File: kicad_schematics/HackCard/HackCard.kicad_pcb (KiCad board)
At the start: 2 copper layers, 43 x 38 mm, 28 parts, among them J10 JST VH B2P, J3 JST VH B4P, J4 Pin Header 2X6, J5 JST VH B4P, J8 JST VH B3P, J9 JST VH B3P, Q1 BC847B, U1 HEF4093B, U2 HEF4093B

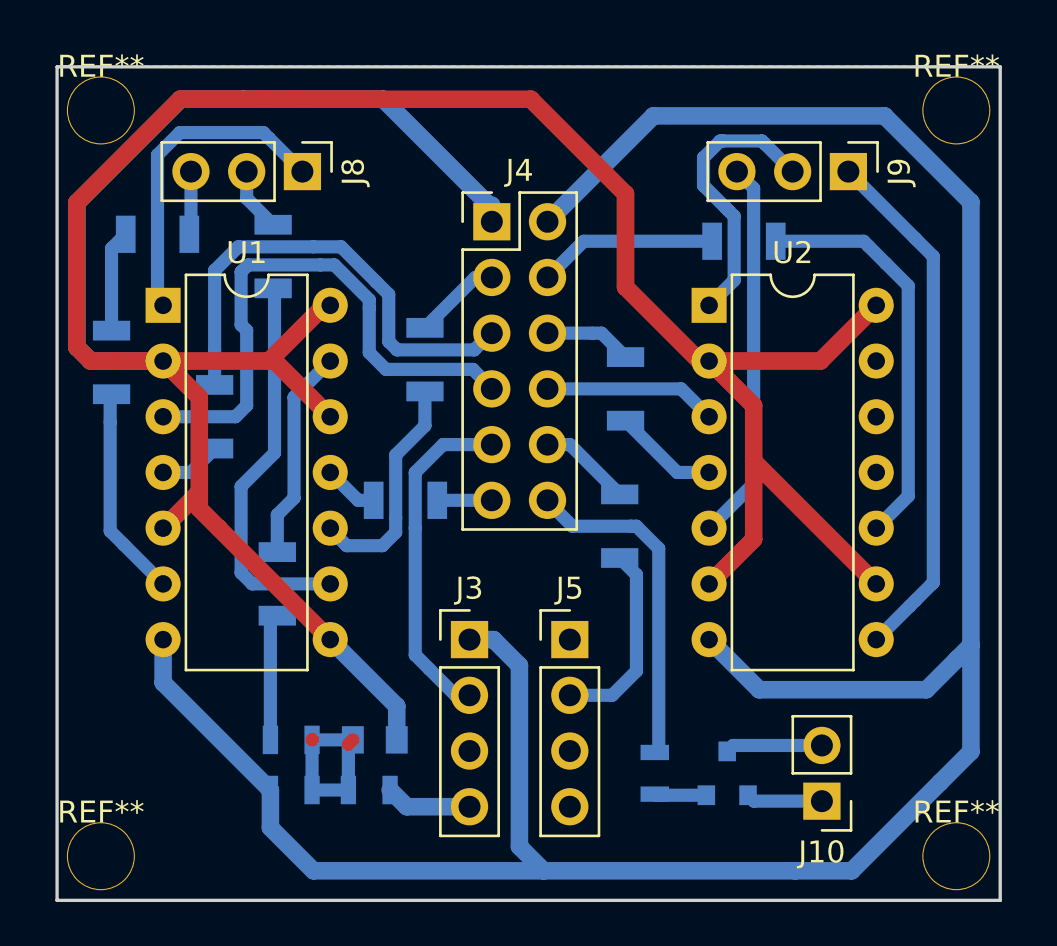
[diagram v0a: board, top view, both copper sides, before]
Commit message: text for I/O
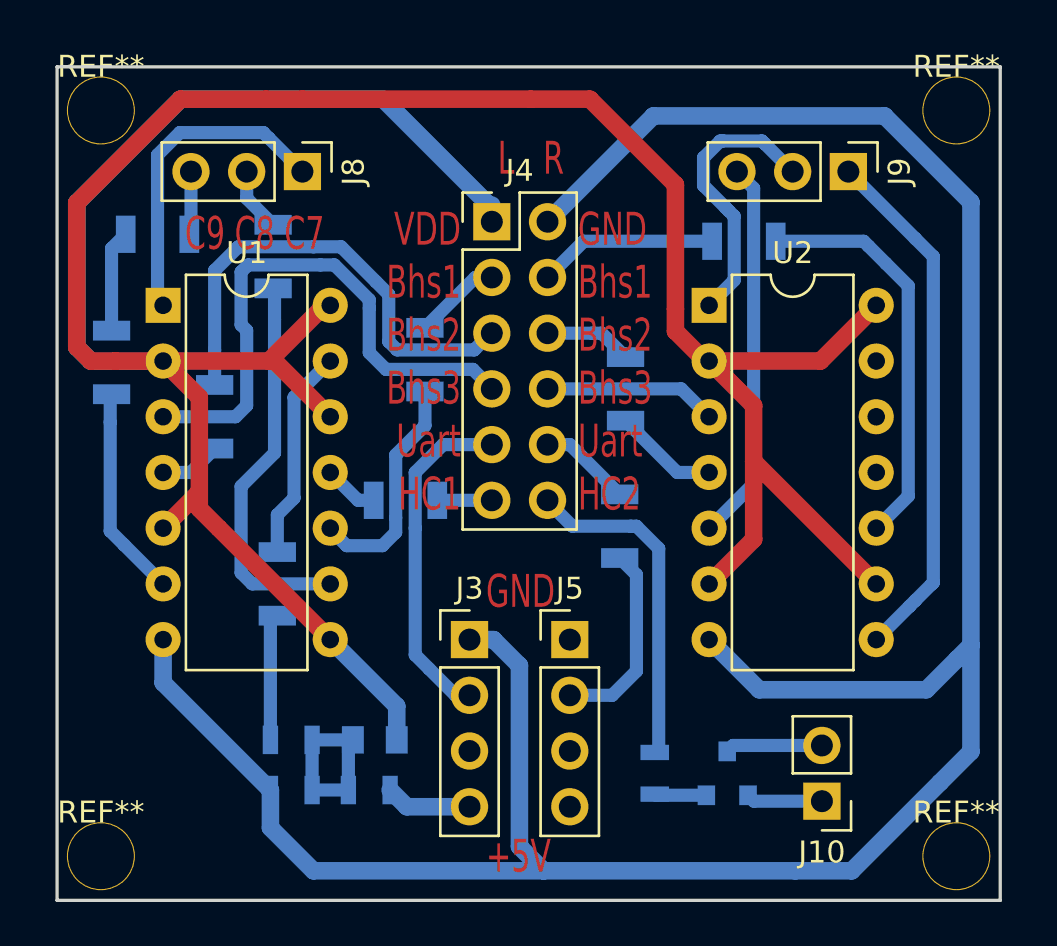
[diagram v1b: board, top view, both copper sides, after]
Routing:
- net VDD: track 149.0 -> 150.9 mm
- removed copper zone on F.Cu, net GND
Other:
- board text added: "C9 C8 C7"
- board text added: "GND +5V"
- board text added: "GND Bhs1 Bhs2 Bhs3 Uart HC2"
- board text added: "L R"
- board text added: "VDD Bhs1 Bhs2 Bhs3 Uart HC1"
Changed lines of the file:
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@@
     (area 96.11657 84.555 168.85943 138.105001)
     (thickness 1.6)
-    (drawings 9)
-    (tracks 213)
+    (drawings 14)
+    (tracks 214)
     (zones 0)
     (modules 28)
@@
     (mod_text_size 1 1)
     (mod_text_width 0.15)
-    (pad_size 3.1 3.1)
-    (pad_drill 3)
+    (pad_size 2 2)
+    (pad_drill 0.8)
     (pad_to_mask_clearance 0.2)
     (aux_axis_origin 0 0)
     (grid_origin 110.988 93.255)
-    (visible_elements FFFEFF7F)
+    (visible_elements FFFCFF7F)
     (pcbplotparams
-      (layerselection 0x00000_80000000)
+      (layerselection 0x00000_00000001)
       (usegerberextensions false)
       (excludeedgelayer false)
@@
       (subtractmaskfromsilk false)
       (outputformat 2)
-      (mirror false)
+      (mirror true)
       (drillshape 2)
       (scaleselection 1)
@@
     (pad 1 thru_hole circle (at 0 0) (size 3.1 3.1) (drill 3) (layers *.Cu *.Mask))
   )
+  (dimension 38 (width 0.3) (layer Eco2.User)
+    (gr_text "38,000 mm" (at 103.638 112.255 90) (layer Eco2.User)
+      (effects (font (size 1.5 1.5) (thickness 0.3)))
+    )
+    (feature1 (pts (xy 110.988 93.255) (xy 102.288 93.255)))
+    (feature2 (pts (xy 110.988 131.255) (xy 102.288 131.255)))
+    (crossbar (pts (xy 104.988 131.255) (xy 104.988 93.255)))
+    (arrow1a (pts (xy 104.988 93.255) (xy 105.574421 94.381504)))
+    (arrow1b (pts (xy 104.988 93.255) (xy 104.401579 94.381504)))
+    (arrow2a (pts (xy 104.988 131.255) (xy 105.574421 130.128496)))
+    (arrow2b (pts (xy 104.988 131.255) (xy 104.401579 130.128496)))
+  )
+  (gr_text "GND\n\n\n\n\n+5V" (at 130.546 123.227) (layer F.Cu)
+    (effects (font (size 1.5 1) (thickness 0.25)) (justify left))
+  )
+  (gr_text "C9 C8 C7" (at 123.18 100.875) (layer F.Cu)
+    (effects (font (size 1.5 1) (thickness 0.25)) (justify right))
+  )
+  (gr_text "L   R" (at 134.102 97.446) (layer F.Cu)
+    (effects (font (size 1.5 1) (thickness 0.25)) (justify right))
+  )
+  (gr_text "GND\nBhs1\nBhs2\nBhs3\nUart\nHC2" (at 134.737 106.717) (layer F.Cu)
+    (effects (font (size 1.5 1) (thickness 0.25)) (justify left))
+  )
+  (gr_text "VDD\nBhs1\nBhs2\nBhs3\nUart\nHC1" (at 129.403 106.717) (layer F.Cu)
+    (effects (font (size 1.5 1) (thickness 0.25)) (justify right))
+  )
   (dimension 3 (width 0.3) (layer Eco2.User)
     (gr_text "3,000 mm" (at 113.488 136.755) (layer Eco2.User)
@@
     (arrow2b (pts (xy 111.488 132.755) (xy 112.614504 132.168579)))
   )
-  (dimension 38 (width 0.3) (layer Eco2.User)
-    (gr_text "38,000 mm" (at 103.638 112.255 270) (layer Eco2.User)
-      (effects (font (size 1.5 1.5) (thickness 0.3)))
-    )
-    (feature1 (pts (xy 110.988 131.255) (xy 102.288 131.255)))
-    (feature2 (pts (xy 110.988 93.255) (xy 102.288 93.255)))
-    (crossbar (pts (xy 104.988 93.255) (xy 104.988 131.255)))
-    (arrow1a (pts (xy 104.988 131.255) (xy 104.401579 130.128496)))
-    (arrow1b (pts (xy 104.988 131.255) (xy 105.574421 130.128496)))
-    (arrow2a (pts (xy 104.988 93.255) (xy 104.401579 94.381504)))
-    (arrow2b (pts (xy 104.988 93.255) (xy 105.574421 94.381504)))
-  )
   (dimension 34 (width 0.3) (layer Eco2.User)
     (gr_text "34,000 mm" (at 106.638 112.255 90) (layer Eco2.User)
@@
   (gr_line (start 153.99 131.268) (end 110.99 131.268) (angle 90) (layer Edge.Cuts) (width 0.15))
   (gr_line (start 153.99 93.268) (end 153.99 131.268) (angle 90) (layer Edge.Cuts) (width 0.15))
-  (segment (start 122.632 123.936) (end 122.616 123.952) (width 0.6) (layer F.Cu) (net 0))
-  (segment (start 124.272 124.156) (end 124.476 123.952) (width 0.6) (layer F.Cu) (net 0))
+  (segment (start 139.182 104.304) (end 139.182 105.32) (width 0.8) (layer F.Cu) (net 1))
+  (segment (start 139.182 105.32) (end 140.542 106.68) (width 0.8) (layer F.Cu) (net 1))
+  (segment (start 140.542 106.68) (end 140.716 106.68) (width 0.8) (layer F.Cu) (net 1))
+  (segment (start 132.578 94.742) (end 135.282 94.742) (width 0.8) (layer F.Cu) (net 1))
+  (segment (start 139.182 98.642) (end 139.182 104.304) (width 0.8) (layer F.Cu) (net 1))
+  (segment (start 135.282 94.742) (end 139.182 98.642) (width 0.8) (layer F.Cu) (net 1))
   (segment (start 120.513 94.742) (end 116.613 94.742) (width 0.8) (layer F.Cu) (net 1))
   (segment (start 116.613 94.742) (end 111.887 99.468) (width 0.8) (layer F.Cu) (net 1))
@@
   (segment (start 111.887 106.045) (end 112.522 106.68) (width 0.8) (layer F.Cu) (net 1))
   (segment (start 112.522 106.68) (end 113.665 106.68) (width 0.8) (layer F.Cu) (net 1))
-  (segment (start 136.906 103.3145) (end 140.2715 106.68) (width 0.8) (layer F.Cu) (net 1))
   (segment (start 122.174 94.742) (end 120.513 94.742) (width 0.8) (layer F.Cu) (net 1))
-  (segment (start 132.588 94.742) (end 122.174 94.742) (width 0.8) (layer F.Cu) (net 1))
-  (segment (start 136.906 99.06) (end 132.588 94.742) (width 0.8) (layer F.Cu) (net 1))
-  (segment (start 136.906 103.3145) (end 136.906 99.06) (width 0.8) (layer F.Cu) (net 1))
+  (segment (start 132.578 94.742) (end 122.174 94.742) (width 0.8) (layer F.Cu) (net 1))
   (segment (start 130.81 100.33) (end 130.81 99.568) (width 0.8) (layer B.Cu) (net 1))
   (segment (start 117.475 112.649) (end 117.475 113.411) (width 0.8) (layer F.Cu) (net 1))
@@
     (connect_pads (clearance 0.508))
     (min_thickness 0.254)
-    (fill yes (arc_segments 16) (thermal_gap 0.508) (thermal_bridge_width 0.508))
-    (polygon
-      (pts
-        (xy 153.988 131.255) (xy 110.988 131.255) (xy 110.988 93.255) (xy 153.988 93.255)
-      )
-    )
-  )
-  (zone (net 7) (net_name GND) (layer F.Cu) (hatch edge 0.508)
-    (connect_pads (clearance 0.508))
-    (min_thickness 0.254)
